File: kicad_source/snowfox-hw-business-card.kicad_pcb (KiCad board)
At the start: 2 copper layers, 85 x 54 mm, 108 parts, among them CN1 Micro_SDCard, CN2 CONN_02X05, CN3 CONN_01X24, CN4 USB_OTG, CN5 CONN_01X14, CN6 CONN_01X04, Q1 SI1304BDL, Q2 BC847, SW1 TAST_VER, SW2 TAST_VER, SW3 TAST_VER, SW4 TAST_VER, SW5 SWITCH_INV, U1 W25Q80D, U2 ATECC608A, U3 FE310-G002, U4 FT230XS, U5 TPS736XX, U6 TPS736XX, U7 M24LR, U8 BMA400, Y1 16MHz

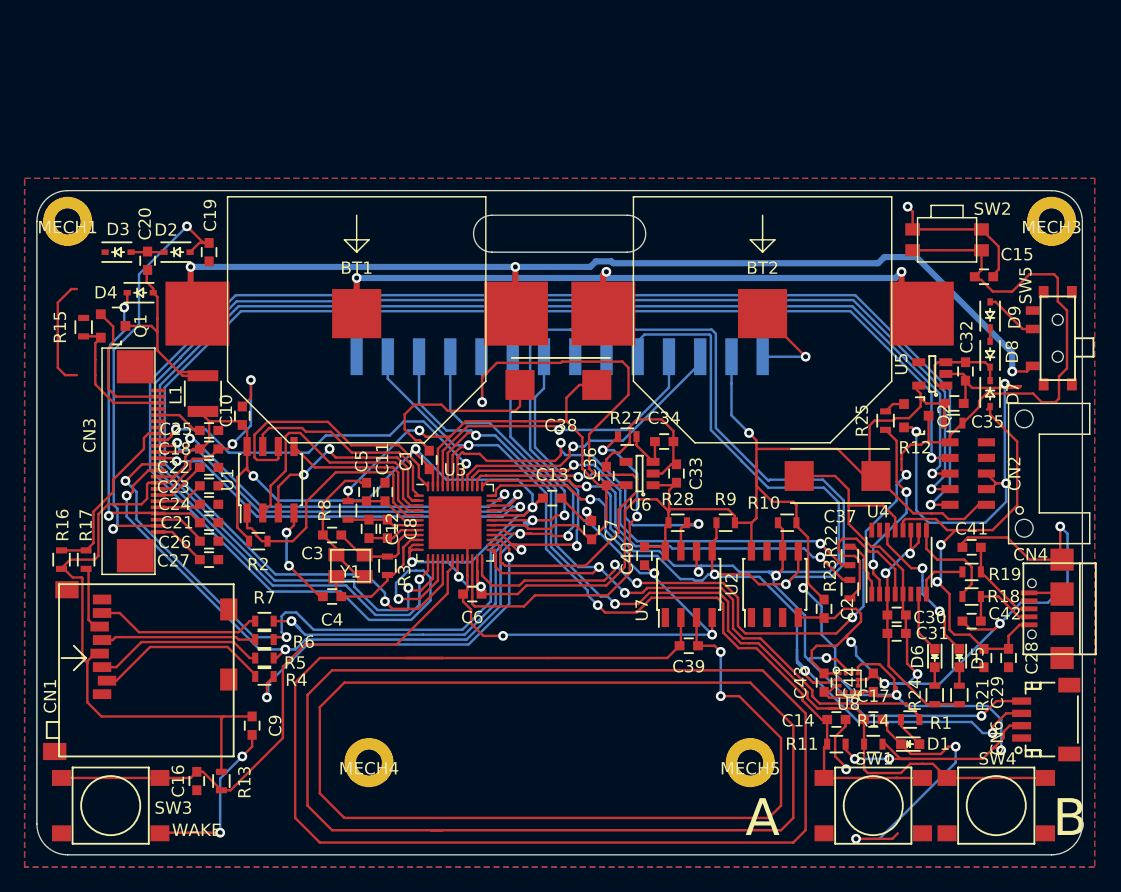
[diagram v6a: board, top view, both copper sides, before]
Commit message: changed wake button to smaller type, moved button A to left side, made some layout
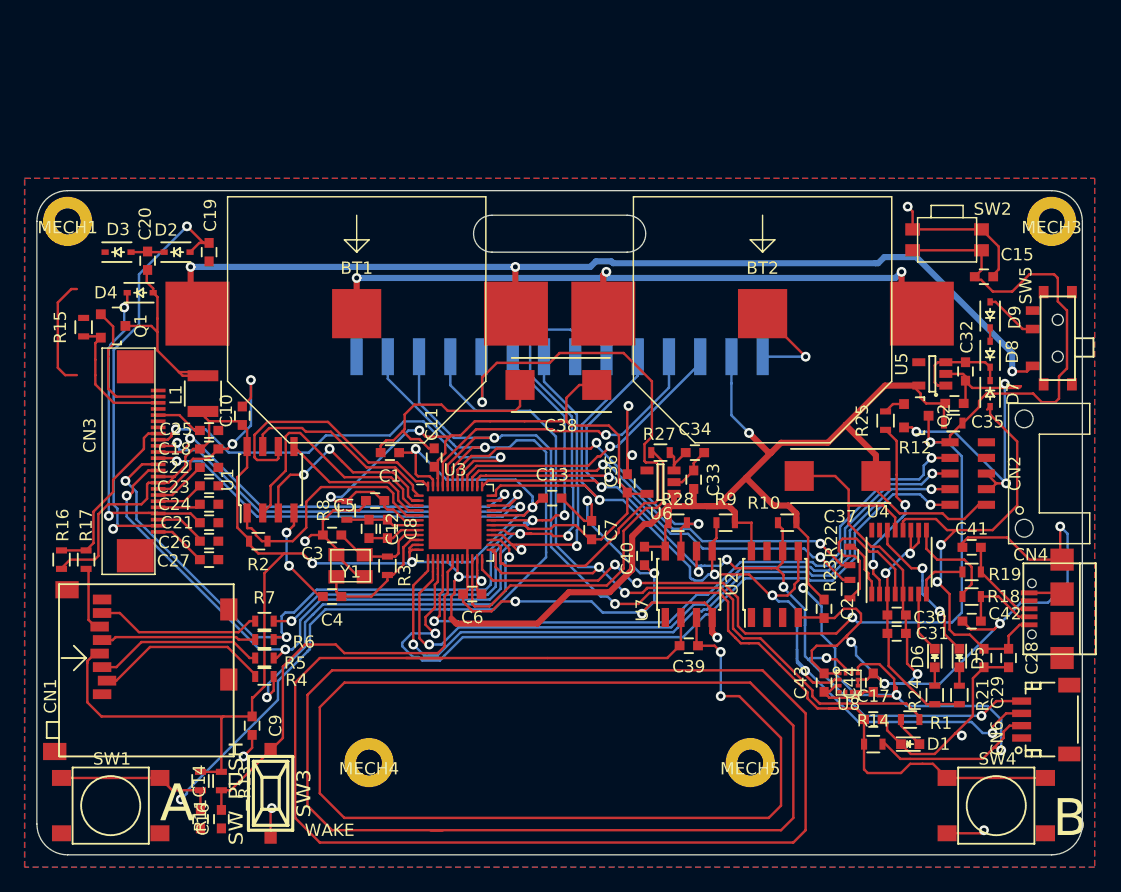
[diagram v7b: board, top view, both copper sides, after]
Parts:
- SW3: value TAST_VER -> SW_PUSH; footprint mechanical-switches:WE_430182050816 -> mechanical-switches:smd_push
- moved SW1 62.0 mm to (84.0, 133.0)
- moved C14 52.3 mm to (91.3, 134.1), turned to 270 degrees
- moved R11 51.8 mm to (91.3, 131.0), turned to 90 degrees
- moved SW3 13.0 mm to (97.0, 132.0), turned to 270 degrees
- moved C11 4.88 mm to (110.3, 104.7)
- moved C16 3.69 mm to (93.0, 134.1)
- moved C1 3.26 mm to (106.7, 104.3), turned to 180 degrees
- moved R27 3.00 mm to (128.7, 104.3)
- moved C34 2.66 mm to (131.5, 104.3)
- moved U6 1.84 mm to (128.7, 106.7)
- moved C36 1.80 mm to (126.0, 106.8)
- moved C33 1.49 mm to (131.4, 106.5)
- moved C5 0.99 mm to (105.5, 108.2), turned to 180 degrees
- moved R8 0.10 mm to (103.2, 109.0)
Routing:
- net /Microcontroller/JTAG_TMS: track 130.7 -> 62.5 mm
- net /Microcontroller/JTAG_TCK: track 117.7 -> 59.2 mm
- net /Microcontroller/JTAG_TDO: track 114.9 -> 57.5 mm
- net /Microcontroller/JTAG_TDI: track 111.5 -> 54.8 mm
- net I2C_SDA: track 117.4 -> 85.6 mm
- net I2C_SCL: track 107.4 -> 80.2 mm, vias 5 -> 6
- net GND: track 327.5 -> 303.3 mm, vias 23 -> 26
- net /Microcontroller/BUTTON_A: track 71.9 -> 85.4 mm
- net /Microcontroller/WAKE: track 45.2 -> 35.9 mm
- net +1V8: track 59.2 -> 67.8 mm
- net RESET: track 96.7 -> 103.8 mm
- net DIS_BUSY: track 30.7 -> 36.2 mm
- net +3V3: track 298.4 -> 301.9 mm, vias 12 -> 10
- net NFC_BUSY: track 31.6 -> 28.2 mm
- net /Microcontroller/BUTTON_B: track 81.9 -> 84.7 mm
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
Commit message: corrected some part numbers
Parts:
- C1, C10, C11, C12, C13, C14, C15, C16, C17, C2, C29, C31, C43, C44, C7, C8, C9: value 100n -> 100nF
- C18, C19, C20, C21, C22, C23, C24, C25, C26: value 1u 50V -> 1uF 50V
- C27: value 470n 50V -> 470nF 50V
- C28, C30, C5, C6: value 10u -> 10uF
- C3, C4: value 15p -> 15pF
- C32, C33, C34, C35, C36: value 1u -> 1uF
- C37, C38: value 100u/6.3V -> 100uF 6.3V
- D1: value blue -> 150060BS75000
- D5: value green -> 150060GS75000
- D6: value red -> 150060RS75000
- R8: value 100 -> 100R
